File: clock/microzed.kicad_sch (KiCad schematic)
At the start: 21 parts, among them P401 CONN_01X10, Q401 BSS138, Q402 BSS138, U401 74LVC541

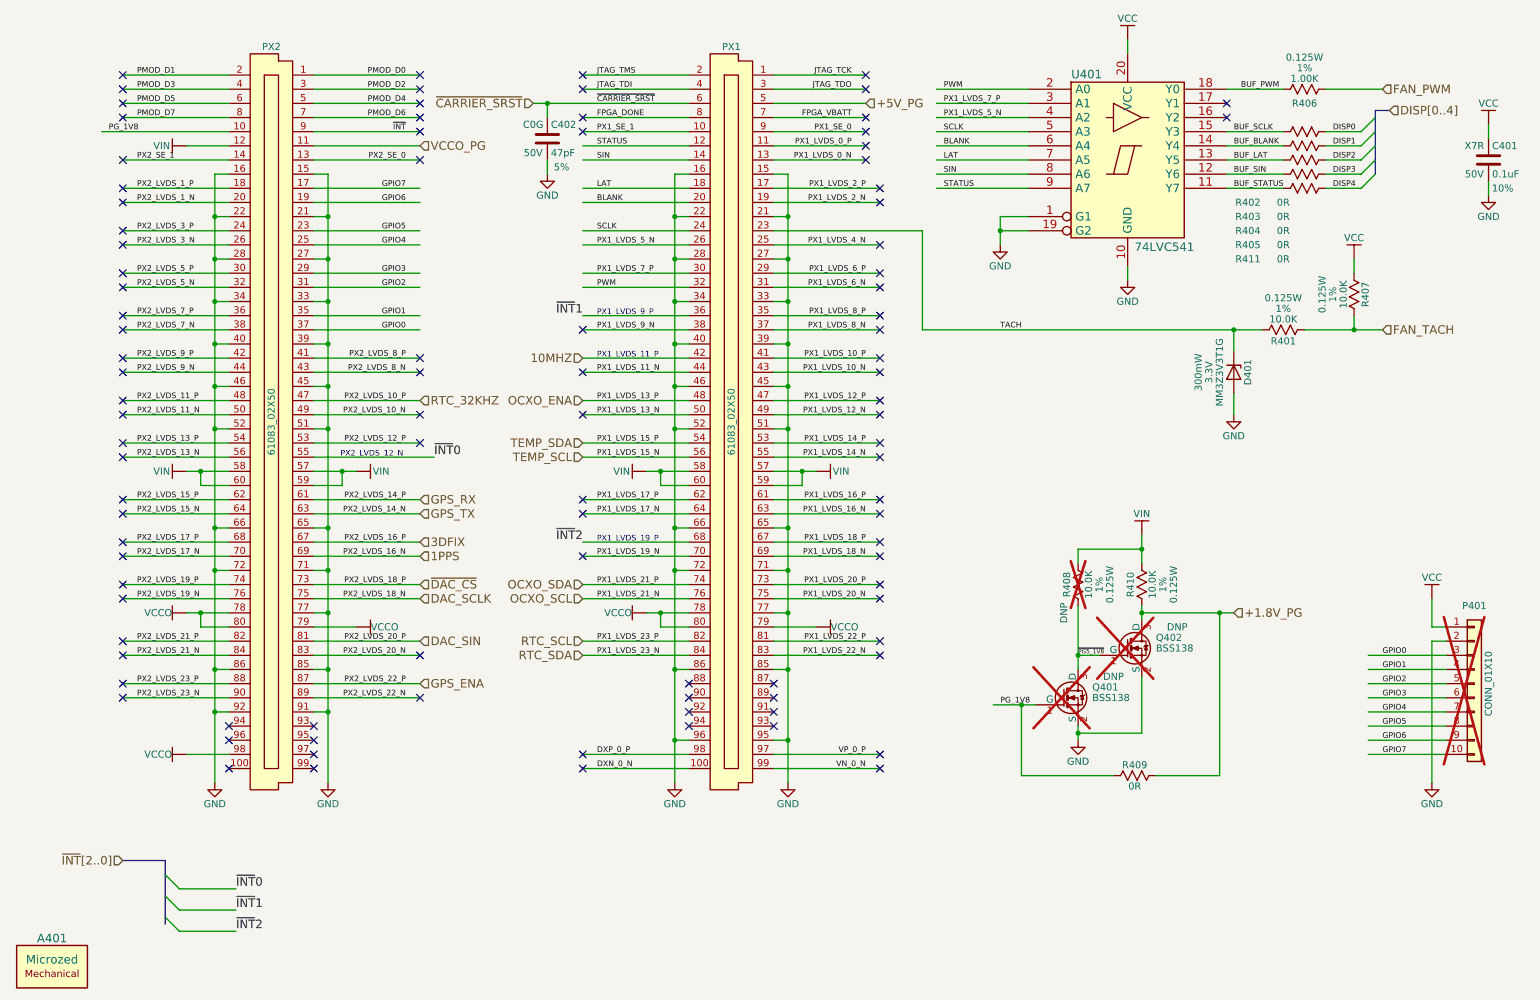
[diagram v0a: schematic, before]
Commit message: Make some net names consistent with hierarchy names. Clean up some silkscreen DRCs.
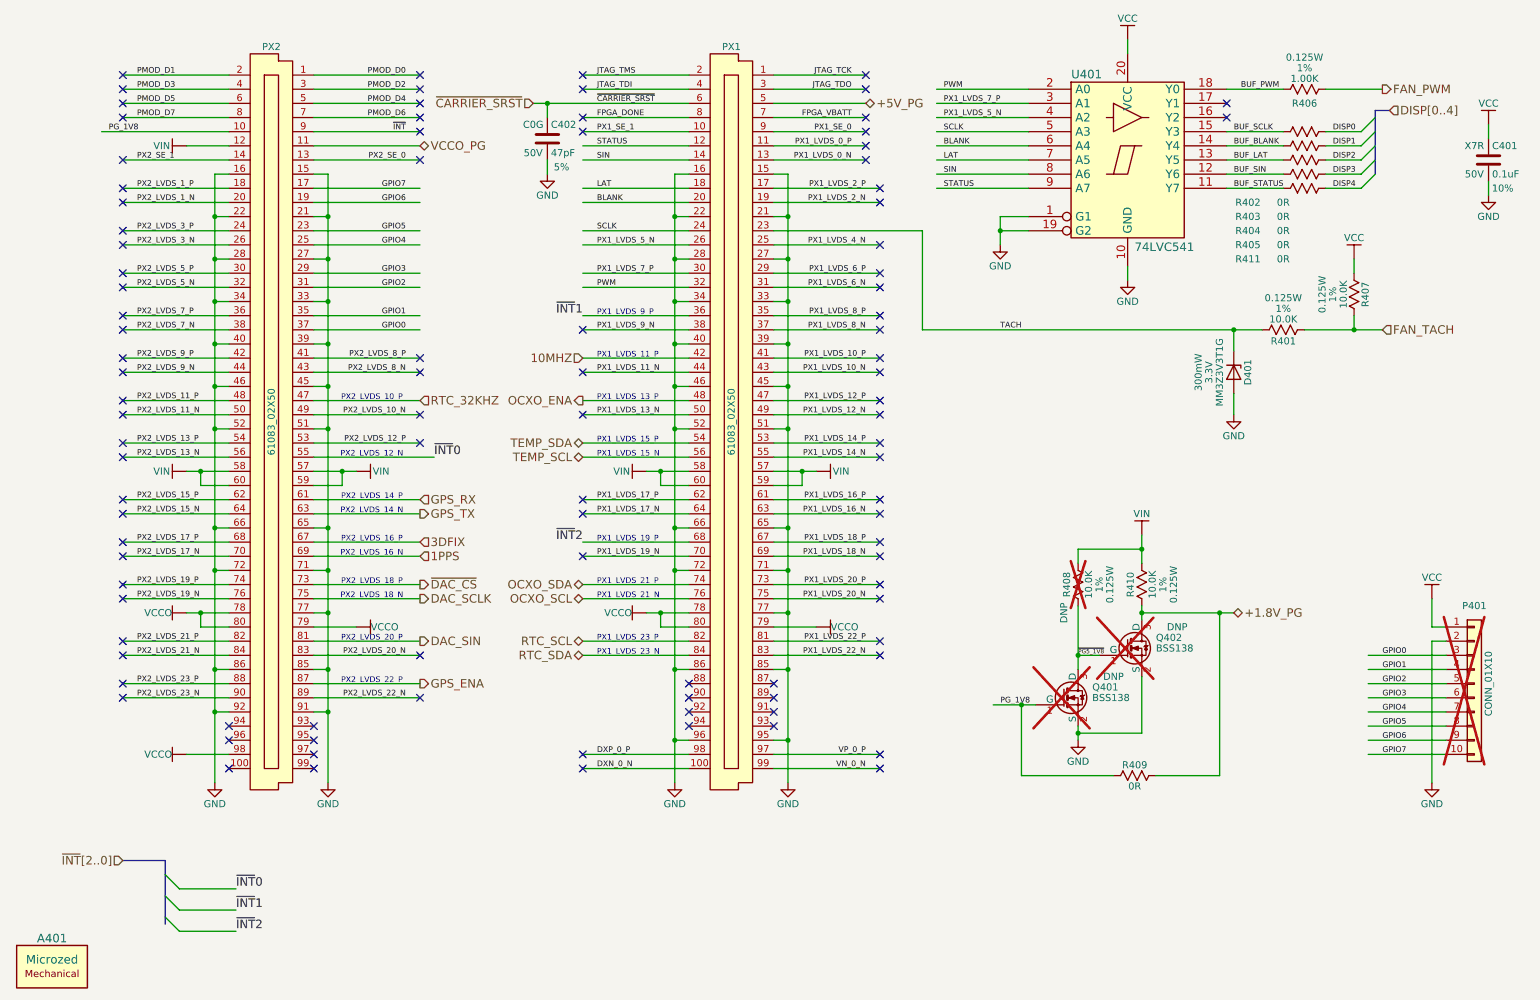
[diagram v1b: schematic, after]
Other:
- note added: "PX1_LVDS_13_P"
- note added: "PX1_LVDS_15_N"
- note added: "PX1_LVDS_15_P"
- note added: "PX1_LVDS_21_N"
- note added: "PX1_LVDS_21_P"
- note added: "PX1_LVDS_23_N"
- note added: "PX1_LVDS_23_P"
- note added: "PX2_LVDS_10_P"
- note added: "PX2_LVDS_14_N"
- note added: "PX2_LVDS_14_P"
- note added: "PX2_LVDS_16_N"
- note added: "PX2_LVDS_16_P"
- note added: "PX2_LVDS_18_N"
- note added: "PX2_LVDS_18_P"
- note added: "PX2_LVDS_20_P"
- note added: "PX2_LVDS_22_P"
